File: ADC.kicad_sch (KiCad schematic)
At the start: 74 parts, among them IC1 ADC0820BCWMX_NOPB, IC2 LCMXO3LF-1300C-5TG100C, IC3 LP38692MPX-3.3_NOPB, IC4 LP38692MPX-5.0_NOPB, J1 Conn_01x06

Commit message: Start of Rev 5. Mimic'd the operation of Rev 3 where 3.3V goes to one side of the switches and a pulldown resistor bank is used on the FPGA input lines. Fixing ERC errors
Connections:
- net 3.3V: now also S1.1, S1.2, S1.3, S1.4, S1.5, S1.6, S1.7, S1.8
- net S0: now also R1.1
- net S1: now also R2.1
- net S2: now also R3.1
- net S3: now also R4.1
- net S4: now also R5.1
- net S5: now also R6.1
- net S6: now also R7.1
- net S7: now also R8.1
- no-connect marks 2 -> 45
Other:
- moved on the sheet: S1

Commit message: Re-created schematic library
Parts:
- C1, C10, C11, C12, C13, C14, C15, C16, C17, C18, C19, C2, C20, C21, C22, C23, C24, C25, C26, C27, C28, C29, C3, C30, C4, C5, C6, C7, C8, C9: symbol Device:C -> ADC_Library:C
- D1, D10, D2, D3, D4, D5, D6, D7, D8, D9: symbol Device:LED -> ADC_Library:LED
- IC1: symbol ADC Project Symbols:ADC0820BCWMX_NOPB -> ADC_Library:ADC0820BCWMX_NOPB
- IC2: symbol ADC Project Symbols:LCMXO3LF-640E-5TG100C -> ADC_Library:LCMXO3LF-640E-5TG100C
- IC3: symbol ADC Project Symbols:LP38692MPX-3.3_NOPB -> ADC_Library:LP38692MPX-3.3_NOPB
- IC4: symbol ADC Project Symbols:LP38692MPX-5.0_NOPB -> ADC_Library:LP38692MPX-5.0_NOPB
- J1: symbol Connector_Generic:Conn_01x06 -> ADC_Library:Conn_01x06
- R1, R10, R11, R12, R13, R14, R15, R16, R17, R18, R19, R2, R3, R4, R5, R6, R7, R8, R9: symbol Device:R -> ADC_Library:R
- S1: symbol ADC Project Symbols:219-8MST -> ADC_Library:219-8MST
- S2: symbol ADC Project Symbols:EVQ-7Q201W -> ADC_Library:EVQ-7Q201W
- TP1, TP2, TP3, TP4: symbol Connector:TestPoint_Alt -> ADC_Library:TestPoint_Alt
- TP5, TP6, TP7: symbol Connector:TestPoint -> ADC_Library:TestPoint
- Y1: symbol ADC Project Symbols:ECS-5032MV-320-BN-TR -> ADC_Library:ECS-5032MV-320-BN-TR

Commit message: Generated fabrication files and moved a few components to pass JLCPCB DFM check
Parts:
- removed TP4: Probe-, TestPoint:TestPoint_THTPad_2.5x2.5mm_Drill1.2mm, symbol ADC_Library:TestPoint_Alt
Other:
- note added: "Probe- possible, but instrumentation amp recommended"
- company: (none) -> LeTourneau University
- title: (none) -> CPGR4233 Voltmeter Project
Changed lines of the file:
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@@
 	(generator_version "10.0")
 	(paper "A4")
+	(title_block
+		(title "CPGR4233 Voltmeter Project")
+		(rev "5")
+		(company "LeTourneau University")
+		(comment 1 "Samuel Johnson, Revised by Allen Morrison")
+	)
 	(text "LEDs"
 		(exclude_from_sim no)
@@
 		)
 	)
+	(text "Probe- possible, but\ninstrumentation amp recommended\n"
+		(exclude_from_sim no)
+		(at 159.258 194.818 0)
+		(effects
+			(font
+				(size 1.27 1.27)
+			)
+		)
+	)
 	(text "RESET BUTTON"
 		(exclude_from_sim no)
@@
 	(wire
 		(pts
-			(xy 162.56 191.77) (xy 162.56 193.04)
-		)
-		(stroke
-			(width 0)
-			(type default)
-		)
-	)
-	(wire
-		(pts
 			(xy 99.06 36.83) (xy 101.6 36.83)
 		)
@@
 	(wire
 		(pts
-			(xy 162.56 193.04) (xy 160.02 193.04)
-		)
-		(stroke
-			(width 0)
-			(type default)
-		)
-	)
-	(wire
-		(pts
 			(xy 156.21 114.3) (xy 171.45 114.3)
 		)
@@
 		)
 	)
-	(global_label "GND"
-		(shape input)
-		(at 160.02 193.04 180)
-		(fields_autoplaced yes)
-		(effects
-			(font
-				(size 1.27 1.27)
-			)
-			(justify right)
-		)
-		(property "Intersheetrefs" "${INTERSHEET_REFS}"
-			(at 153.1643 193.04 0)
-			(hide yes)
-			(show_name no)
-			(do_not_autoplace no)
-			(effects
-				(font
-					(size 1.27 1.27)
-				)
-				(justify right)
-			)
-		)
-	)
 	(global_label "3.3V"
 		(shape input)
@@
 					(unit 1)
 				)
-			)
-		)
-	)
-	(symbol
-		(lib_id "ADC_Library:TestPoint_Alt")
-		(at 162.56 191.77 0)
-		(unit 1)
-		(body_style 1)
-		(exclude_from_sim no)
-		(in_bom yes)
-		(on_board no)
-		(in_pos_files yes)
-		(dnp no)
-		(property "Reference" "TP4"
-			(at 165.1 187.1979 0)
-			(show_name no)
-			(do_not_autoplace no)
-			(effects
-				(font
-					(size 1.27 1.27)
-				)
-				(justify left)
-			)
-		)
-		(property "Value" "Probe-"
-			(at 165.1 189.7379 0)
-			(show_name no)
-			(do_not_autoplace no)
-			(effects
-				(font
-					(size 1.27 1.27)
-				)
-				(justify left)
-			)
-		)
-		(property "Footprint" "TestPoint:TestPoint_THTPad_2.5x2.5mm_Drill1.2mm"
-			(at 167.64 191.77 0)
-			(hide yes)
-			(show_name no)
-			(do_not_autoplace no)
-			(effects
-				(font
-					(size 1.27 1.27)
-				)
-			)
-		)
-		(property "Datasheet" ""
-			(at 167.64 191.77 0)
-			(hide yes)
-			(show_name no)
-			(do_not_autoplace no)
-			(effects
-				(font
-					(size 1.27 1.27)
-				)
-			)
-		)
-		(property "Description" "test point (alternative shape)"
-			(at 162.56 191.77 0)
-			(hide yes)
-			(show_name no)
-			(do_not_autoplace no)
-			(effects
-				(font
-					(size 1.27 1.27)
-				)
-			)
-		)
-		(property "Manufacturer_Name" "Keystone Electronics"
-			(at 162.56 191.77 0)
-			(hide yes)
-			(show_name no)
-			(do_not_autoplace no)
-			(effects
-				(font
-					(size 1.27 1.27)
-				)
-			)
-		)
-		(property "Manufacturer_Part_Number" "4952"
-			(at 162.56 191.77 0)
-			(hide yes)
-			(show_name no)
-			(do_not_autoplace no)
-			(effects
-				(font
-					(size 1.27 1.27)
-				)
-			)
-		)
-		(pin "1"
-		)
-		(instances
-			(project "ADC"
-				(path "/e7970bbe-713a-4171-baeb-97713fa53b7a"
-					(reference "TP4")
-					(unit 1)
-				)

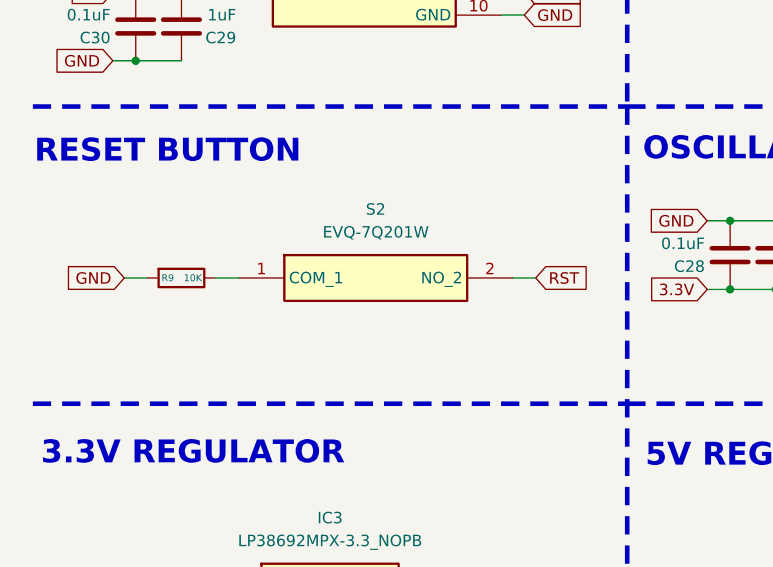
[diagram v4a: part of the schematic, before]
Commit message: Rewired reset switch to toggle between grounded reset pin and VCC. Corrected some symbol errors
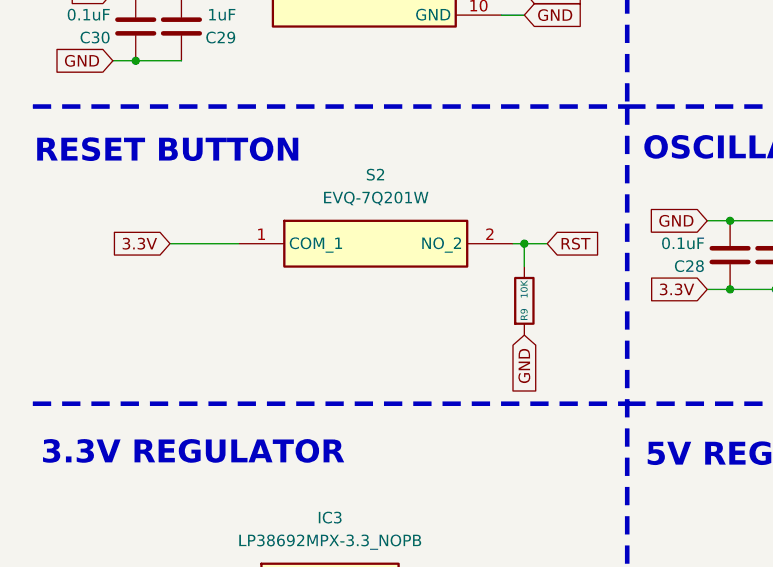
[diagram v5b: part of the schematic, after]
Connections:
- net 3.3V: now also S2.1 (COM_1)
- net RST: now also R9.1
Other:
- moved on the sheet: S2
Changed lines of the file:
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@@
 	)
 	(junction
+		(at 67.31 82.55)
+		(diameter 0)
+		(color 0 0 0 0)
+	)
+	(junction
 		(at 179.07 24.13)
 		(diameter 0)
@@
 	(wire
 		(pts
+			(xy 67.31 82.55) (xy 69.85 82.55)
+		)
+		(stroke
+			(width 0)
+			(type default)
+		)
+	)
+	(wire
+		(pts
 			(xy 99.06 24.13) (xy 99.06 26.67)
 		)
@@
 	(wire
 		(pts
+			(xy 67.31 82.55) (xy 67.31 85.09)
+		)
+		(stroke
+			(width 0)
+			(type default)
+		)
+	)
+	(wire
+		(pts
 			(xy 30.48 125.73) (xy 33.02 125.73)
 		)
@@
 	(wire
 		(pts
-			(xy 22.86 86.36) (xy 25.4 86.36)
+			(xy 27.94 82.55) (xy 35.56 82.55)
 		)
 		(stroke
@@
 	(wire
 		(pts
-			(xy 66.04 86.36) (xy 68.58 86.36)
+			(xy 66.04 82.55) (xy 67.31 82.55)
 		)
 		(stroke
@@
 	(wire
 		(pts
-			(xy 33.02 86.36) (xy 35.56 86.36)
-		)
-		(stroke
-			(width 0)
-			(type default)
-		)
-	)
-	(wire
-		(pts
 			(xy 64.77 52.07) (xy 67.31 52.07)
 		)
@@
 		)
 	)
+	(global_label "3.3V"
+		(shape input)
+		(at 27.94 82.55 180)
+		(fields_autoplaced yes)
+		(effects
+			(font
+				(size 1.27 1.27)
+			)
+			(justify right)
+		)
+		(property "Intersheetrefs" "${INTERSHEET_REFS}"
+			(at 20.8424 82.55 0)
+			(hide yes)
+			(show_name no)
+			(do_not_autoplace no)
+			(effects
+				(font
+					(size 1.27 1.27)
+				)
+				(justify right)
+			)
+		)
+	)
 	(global_label "GND"
 		(shape input)
@@
 		)
 	)
-	(global_label "GND"
-		(shape input)
-		(at 22.86 86.36 180)
-		(fields_autoplaced yes)
-		(effects
-			(font
-				(size 1.27 1.27)
-			)
-			(justify right)
-		)
-		(property "Intersheetrefs" "${INTERSHEET_REFS}"
-			(at 16.0043 86.36 0)
-			(hide yes)
-			(show_name no)
-			(do_not_autoplace no)
-			(effects
-				(font
-					(size 1.27 1.27)
-				)
-				(justify right)
-			)
-		)
-	)
 	(global_label "D3"
 		(shape input)
@@
 	(global_label "RST"
 		(shape input)
-		(at 68.58 86.36 0)
+		(at 69.85 82.55 0)
 		(fields_autoplaced yes)
 		(effects
@@
 		)
 		(property "Intersheetrefs" "${INTERSHEET_REFS}"
-			(at 75.0123 86.36 0)
+			(at 76.2823 82.55 0)
 			(hide yes)
 			(show_name no)
@@
 		)
 	)
+	(global_label "GND"
+		(shape input)
+		(at 67.31 92.71 270)
+		(fields_autoplaced yes)
+		(effects
+			(font
+				(size 1.27 1.27)
+			)
+			(justify right)
+		)
+		(property "Intersheetrefs" "${INTERSHEET_REFS}"
+			(at 67.31 99.5657 90)
+			(hide yes)
+			(show_name no)
+			(do_not_autoplace no)
+			(effects
+				(font
+					(size 1.27 1.27)
+				)
+				(justify right)
+			)
+		)
+	)
 	(global_label "DB5"
 		(shape input)
@@
 	(symbol
 		(lib_id "ADC_Library:R")
-		(at 29.21 86.36 270)
-		(unit 1)
-		(body_style 1)
-		(exclude_from_sim no)
-		(in_bom yes)
-		(on_board yes)
-		(in_pos_files yes)
-		(dnp no)
-		(property "Reference" "R9"
-			(at 27.686 86.36 90)
-			(show_name no)
-			(do_not_autoplace no)
-			(effects
-				(font
-					(size 0.762 0.762)
-				)
-			)
-		)
-		(property "Value" "10K"
-			(at 30.48 86.36 90)
-			(show_name no)
-			(do_not_autoplace no)
-			(effects
-				(font
-					(size 0.762 0.762)
-				)
-			)
-		)
-		(property "Footprint" "Resistor_SMD:R_0805_2012Metric_Pad1.20x1.40mm_HandSolder"
-			(at 29.21 84.582 90)
-			(hide yes)
-			(show_name no)
-			(do_not_autoplace no)
-			(effects
-				(font
-					(size 1.27 1.27)
-				)
-			)
-		)
-		(property "Datasheet" ""
-			(at 29.21 86.36 0)
-			(hide yes)
-			(show_name no)
-			(do_not_autoplace no)
-			(effects
-				(font
-					(size 1.27 1.27)
-				)
-			)
-		)
-		(property "Description" "Resistor"
-			(at 29.21 86.36 0)
-			(hide yes)
-			(show_name no)
-			(do_not_autoplace no)
-			(effects
-				(font
-					(size 1.27 1.27)
-				)
-			)
-		)
-		(property "Manufacturer_Name" "YAGEO"
-			(at 29.21 86.36 90)
-			(hide yes)
-			(show_name no)
-			(do_not_autoplace no)
-			(effects
-				(font
-					(size 1.27 1.27)
-				)
-			)
-		)
-		(property "Manufacturer_Part_Number" "AC0805FR-7W10KL"
-			(at 29.21 86.36 90)
-			(hide yes)
-			(show_name no)
-			(do_not_autoplace no)
-			(effects
-				(font
-					(size 1.27 1.27)
-				)
-			)
-		)
-		(pin "1"
-		)
-		(pin "2"
-		)
-		(instances
-			(project "ADC"
-				(path "/e7970bbe-713a-4171-baeb-97713fa53b7a"
-					(reference "R9")
-					(unit 1)
-				)
-			)
-		)
-	)
-	(symbol
-		(lib_id "ADC_Library:R")
 		(at 36.83 186.69 270)
 		(unit 1)
@@
 	)
 	(symbol
+		(lib_id "ADC_Library:R")
+		(at 67.31 88.9 0)
+		(unit 1)
+		(body_style 1)
+		(exclude_from_sim no)
+		(in_bom yes)
+		(on_board yes)
+		(in_pos_files yes)
+		(dnp no)
+		(property "Reference" "R9"
+			(at 67.31 90.424 90)
+			(show_name no)
+			(do_not_autoplace no)
+			(effects
+				(font
+					(size 0.762 0.762)
+				)
+			)
+		)
+		(property "Value" "10K"
+			(at 67.31 87.63 90)
+			(show_name no)
+			(do_not_autoplace no)
+			(effects
+				(font
+					(size 0.762 0.762)
+				)
+			)
+		)
+		(property "Footprint" "Resistor_SMD:R_0805_2012Metric_Pad1.20x1.40mm_HandSolder"
+			(at 65.532 88.9 90)
+			(hide yes)
+			(show_name no)
+			(do_not_autoplace no)
+			(effects
+				(font
+					(size 1.27 1.27)
+				)
+			)
+		)
+		(property "Datasheet" ""
+			(at 67.31 88.9 0)
+			(hide yes)
+			(show_name no)
+			(do_not_autoplace no)
+			(effects
+				(font
+					(size 1.27 1.27)
+				)
+			)
+		)
+		(property "Description" "Resistor"
+			(at 67.31 88.9 0)
+			(hide yes)
+			(show_name no)
+			(do_not_autoplace no)
+			(effects
+				(font
+					(size 1.27 1.27)
+				)
+			)
+		)
+		(property "Manufacturer_Name" "YAGEO"
+			(at 67.31 88.9 90)
+			(hide yes)
+			(show_name no)
+			(do_not_autoplace no)
+			(effects
+				(font
+					(size 1.27 1.27)
+				)
+			)
+		)
+		(property "Manufacturer_Part_Number" "AC0805FR-7W10KL"
+			(at 67.31 88.9 90)
+			(hide yes)
+			(show_name no)
+			(do_not_autoplace no)
+			(effects
+				(font
+					(size 1.27 1.27)
+				)
+			)
+		)
+		(pin "1"
+		)
+		(pin "2"
+		)
+		(instances
+			(project "ADC"
+				(path "/e7970bbe-713a-4171-baeb-97713fa53b7a"
+					(reference "R9")
+					(unit 1)
+				)
+			)
+		)
+	)
+	(symbol
 		(lib_id "ADC_Library:EVQ-7Q201W")
-		(at 35.56 86.36 0)
+		(at 35.56 82.55 0)
 		(unit 1)
 		(body_style 1)
@@
 		(fields_autoplaced yes)
 		(property "Reference" "S2"
-			(at 50.8 78.74 0)
+			(at 50.8 74.93 0)
 			(show_name no)
 			(do_not_autoplace no)
@@
 		)
 		(property "Value" "EVQ-7Q201W"
-			(at 50.8 81.28 0)
+			(at 50.8 77.47 0)
 			(show_name no)
 			(do_not_autoplace no)
@@
 		)
 		(property "Footprint" "Button_Switch_SMD:SW_SPST_EVQQ2"
-			(at 62.23 181.28 0)
+			(at 62.23 177.47 0)
 			(hide yes)
 			(show_name no)
@@
 		)
 		(property "Datasheet" "https://industrial.panasonic.com/cdbs/www-data/pdf/ATK0000/ATK0000C360.pdf"
-			(at 62.23 281.28 0)
+			(at 62.23 277.47 0)
 			(hide yes)
 			(show_name no)
@@
 		)
 		(property "Description" "Tactile Switches 6x6x2mm 0.8N With Grnd Term"
-			(at 35.56 86.36 0)
+			(at 35.56 82.55 0)
 			(hide yes)
 			(show_name no)
@@
 		)
 		(property "Height" "2.2"
-			(at 62.23 481.28 0)
+			(at 62.23 477.47 0)
 			(hide yes)
 			(show_name no)
@@
 		)
 		(property "Mouser Part Number" "667-EVQ-7Q201W"
-			(at 62.23 581.28 0)
+			(at 62.23 577.47 0)
 			(hide yes)
 			(show_name no)
@@
 		)
 		(property "Mouser Price/Stock" "https://www.mouser.co.uk/ProductDetail/Panasonic/EVQ-7Q201W?qs=PzGy0jfpSMtXep4dt4ZPsQ%3D%3D"
-			(at 62.23 681.28 0)
+			(at 62.23 677.47 0)
 			(hide yes)
 			(show_name no)
@@
 		)
 		(property "Manufacturer_Name" "Panasonic"
-			(at 62.23 781.28 0)
+			(at 62.23 777.47 0)
 			(hide yes)
 			(show_name no)
@@
 		)
 		(property "Manufacturer_Part_Number" "EVQ-7Q201W"
-			(at 62.23 881.28 0)
+			(at 62.23 877.47 0)
 			(hide yes)
 			(show_name no)
